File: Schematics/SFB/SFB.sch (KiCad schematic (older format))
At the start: 11 parts, among them J1 JST XH 1x5, SW1 SW_DPST, SW2 SW_DPST, SW3 SW_DPST, U1 Arduino_Nano_v3.x, U2 A1326 LUA-T, U3 A1326 LUA-T, U4 A1326 LUA-T, U5 A1326 LUA-T, U6 A1326 LUA-T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

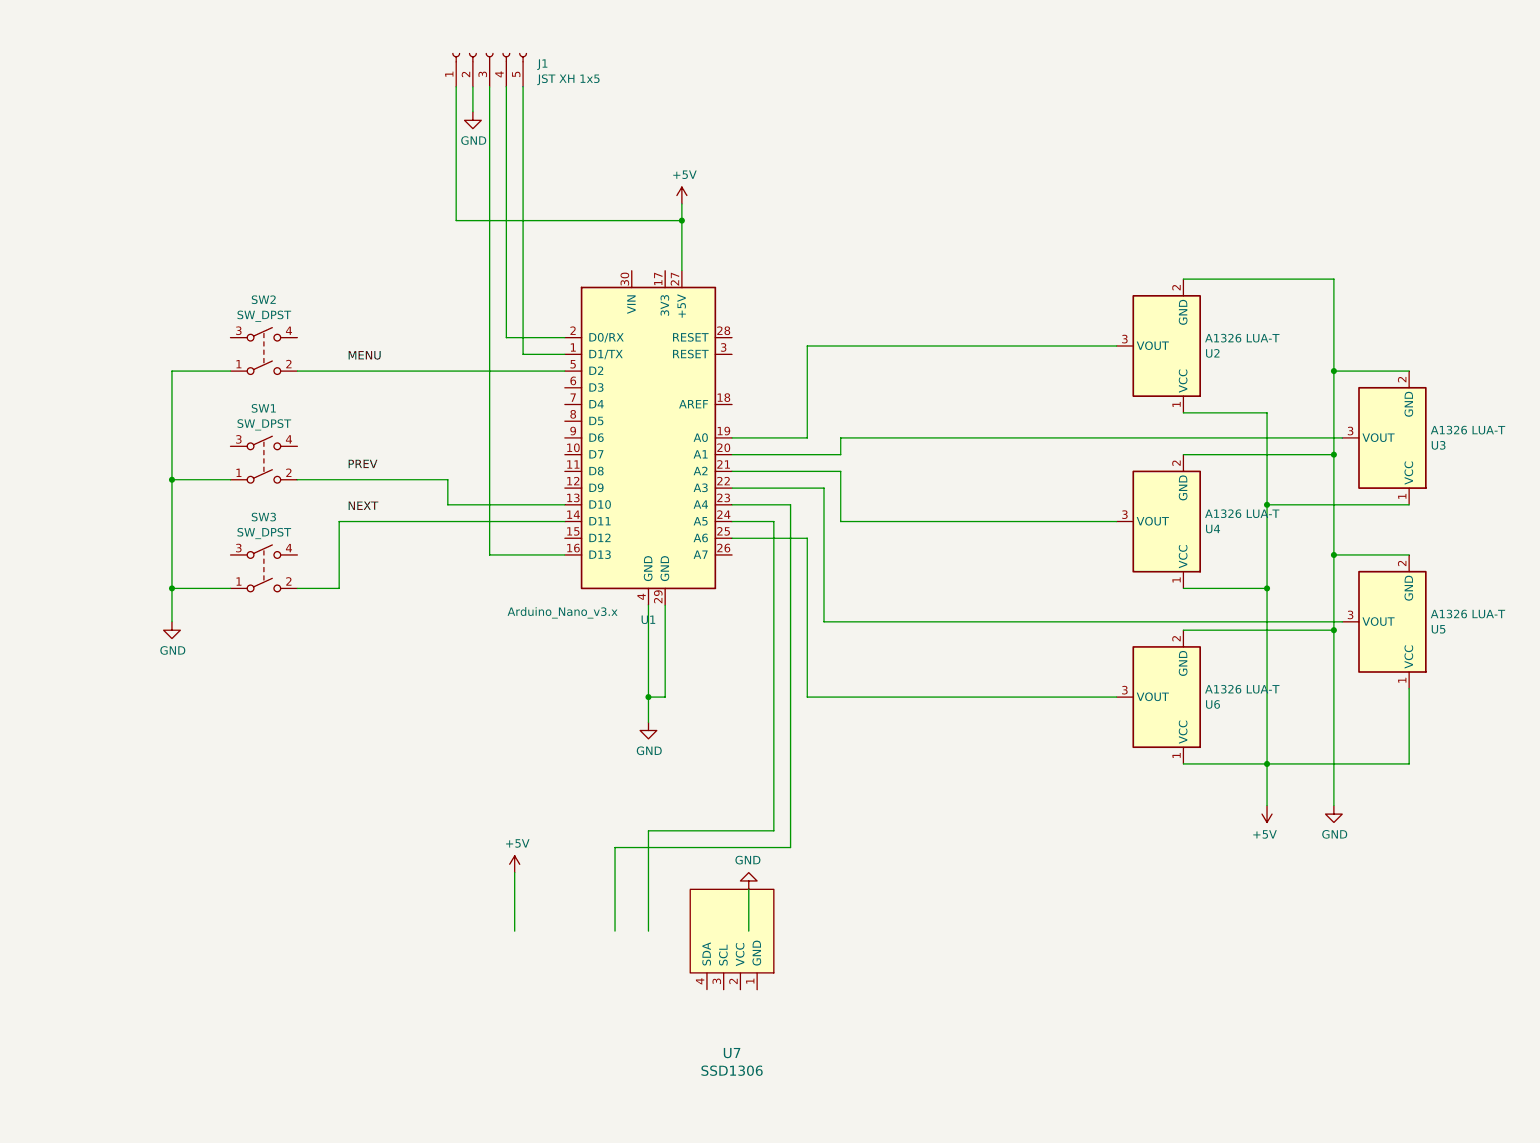
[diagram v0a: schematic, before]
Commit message: Added PCB Rev.2 design
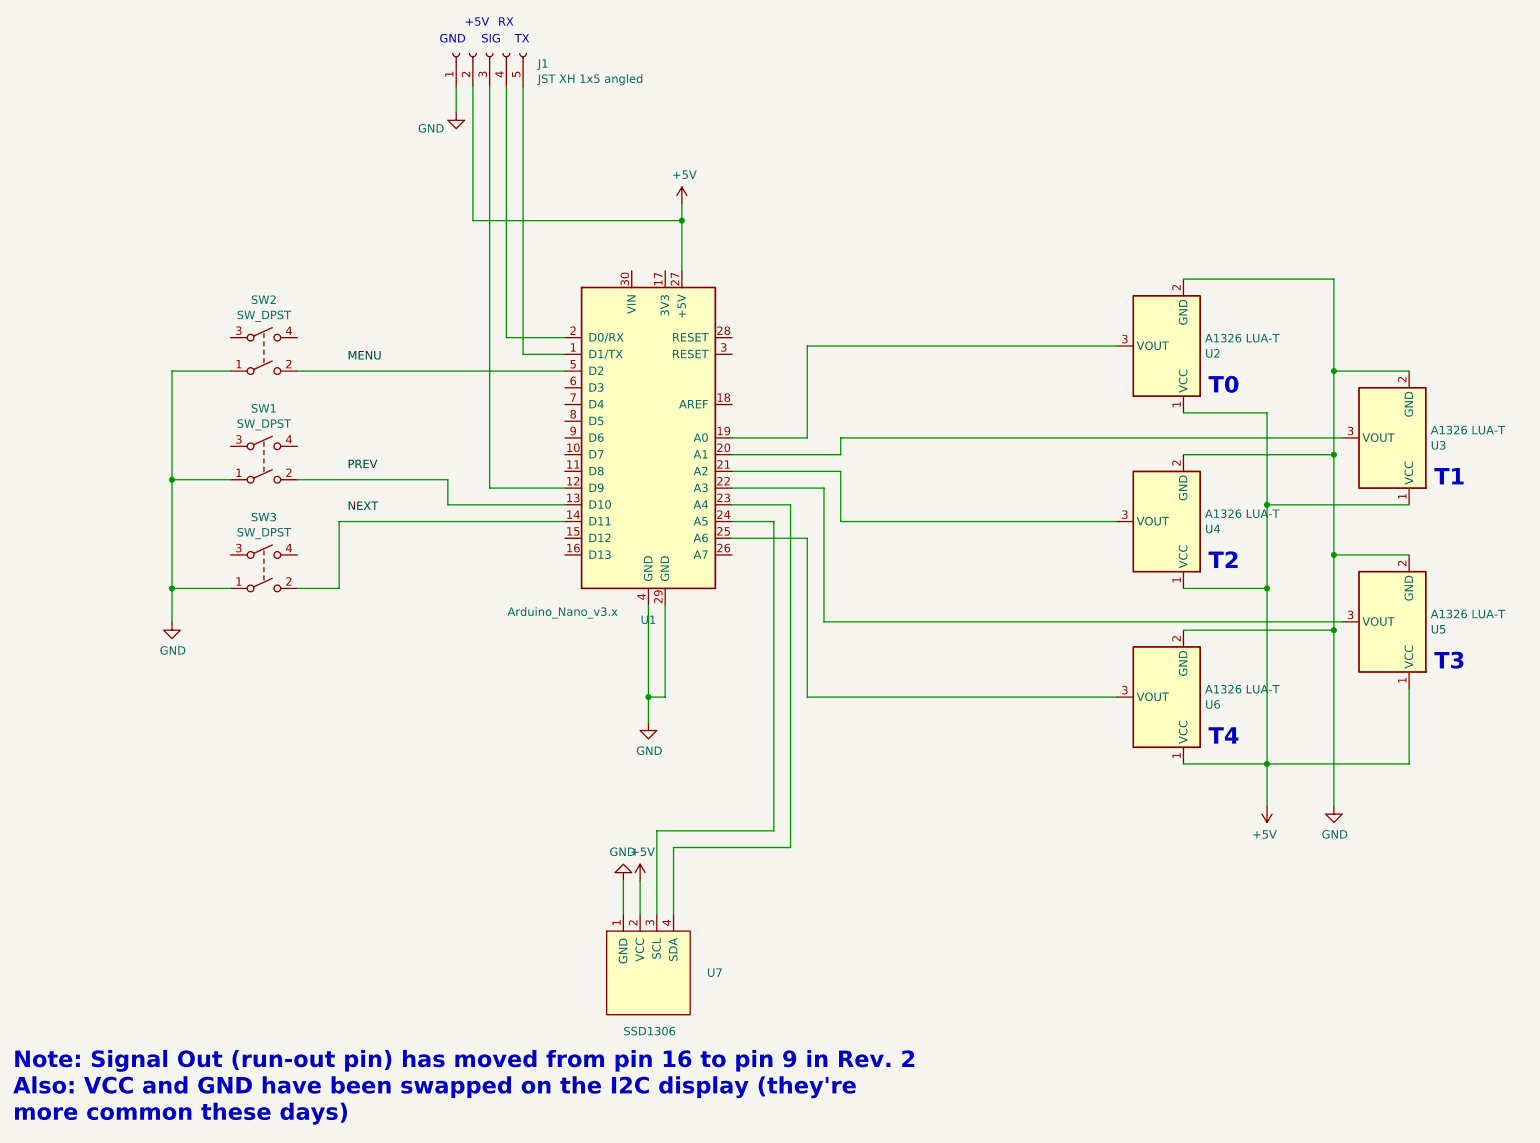
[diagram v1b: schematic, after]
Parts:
- removed U7: SSD1306, symbol SSD1306_OLED-0.91-128x32:SSD1306
- added U7: SSD1306, Connector_PinHeader_2.54mm:PinHeader_1x04_P2.54mm_Vertical, symbol SFB-rescue:SSD1306
- J1: value JST XH 1x5 -> JST XH 1x5 angled; footprint (none) -> Connector_JST:JST_XH_S5B-XH-A_1x05_P2.50mm_Horizontal
- SW1, SW2, SW3: footprint (none) -> SFB:SW_Tactile_Straight_KSA0Axx1LFTR-4Pin
- U2, U3, U4, U5, U6: footprint (none) -> Package_TO_SOT_THT:TO-92Flat
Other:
- note added: "+5V"
- note added: "GND\n"
- note added: "Note: Signal Out (run-out pin) has moved from pin 16 to pin 9 in Rev. 2\nAlso: VCC and GND have been swapped on the I2C display (they're \nmore common these days)"
- note added: "RX"
- note added: "SIG"
- note added: "T0"
- note added: "T1\n"
- note added: "T2"
- note added: "T3"
- note added: "T4"
- note added: "TX"
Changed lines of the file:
@@
 EESchema Schematic File Version 4
+LIBS:SFB-cache
 EELAYER 29 0
 EELAYER END
@@
 Title "Smart Filament Buffer"
 Date "2019-06-24"
-Rev "1"
+Rev "2"
 Comp "Technik Gegg"
 Comment1 ""
@@
 F 0 "U2" H 7321 3096 50  0000 R CNN
 F 1 "A1326 LUA-T" H 7321 3005 50  0000 R CNN
-F 2 "" H 7550 2700 50  0001 L CIN
+F 2 "Package_TO_SOT_THT:TO-92Flat" H 7550 2700 50  0001 L CIN
 F 3 "http://www.allegromicro.com/~/media/Files/Datasheets/A1301-2-Datasheet.ashx" H 7450 3050 50  0001 C CNN
 	1    7550 3050
@@
 F 0 "U4" H 7321 4146 50  0000 R CNN
 F 1 "A1326 LUA-T" H 7321 4055 50  0000 R CNN
-F 2 "" H 7550 3750 50  0001 L CIN
+F 2 "Package_TO_SOT_THT:TO-92Flat" H 7550 3750 50  0001 L CIN
 F 3 "http://www.allegromicro.com/~/media/Files/Datasheets/A1301-2-Datasheet.ashx" H 7450 4100 50  0001 C CNN
 	1    7550 4100
@@
 F 0 "U6" H 7321 5196 50  0000 R CNN
 F 1 "A1326 LUA-T" H 7321 5105 50  0000 R CNN
-F 2 "" H 7550 4800 50  0001 L CIN
+F 2 "Package_TO_SOT_THT:TO-92Flat" H 7550 4800 50  0001 L CIN
 F 3 "http://www.allegromicro.com/~/media/Files/Datasheets/A1301-2-Datasheet.ashx" H 7450 5150 50  0001 C CNN
 	1    7550 5150
@@
 F 0 "U3" H 8671 3646 50  0000 R CNN
 F 1 "A1326 LUA-T" H 8671 3555 50  0000 R CNN
-F 2 "" H 8900 3250 50  0001 L CIN
+F 2 "Package_TO_SOT_THT:TO-92Flat" H 8900 3250 50  0001 L CIN
 F 3 "http://www.allegromicro.com/~/media/Files/Datasheets/A1301-2-Datasheet.ashx" H 8800 3600 50  0001 C CNN
 	1    8900 3600
@@
 F 0 "U5" H 8671 4746 50  0000 R CNN
 F 1 "A1326 LUA-T" H 8671 4655 50  0000 R CNN
-F 2 "" H 8900 4350 50  0001 L CIN
+F 2 "Package_TO_SOT_THT:TO-92Flat" H 8900 4350 50  0001 L CIN
 F 3 "http://www.allegromicro.com/~/media/Files/Datasheets/A1301-2-Datasheet.ashx" H 8800 4700 50  0001 C CNN
 	1    8900 4700
@@
 $EndComp
 $Comp
-L power:GND #PWR?
+L power:GND #PWR0101
 U 1 1 5D10FB78
 P 8550 5800
-F 0 "#PWR?" H 8550 5550 50  0001 C CNN
+F 0 "#PWR0101" H 8550 5550 50  0001 C CNN
 F 1 "GND" H 8555 5627 50  0000 C CNN
 F 2 "" H 8550 5800 50  0001 C CNN
@@
 $EndComp
 $Comp
-L power:GND #PWR?
+L power:GND #PWR0102
 U 1 1 5D11026E
 P 4450 5300
-F 0 "#PWR?" H 4450 5050 50  0001 C CNN
+F 0 "#PWR0102" H 4450 5050 50  0001 C CNN
 F 1 "GND" H 4455 5127 50  0000 C CNN
 F 2 "" H 4450 5300 50  0001 C CNN
@@
 	5400 4200 4950 4200
 $Comp
-L power:+5V #PWR?
+L power:+5V #PWR0103
 U 1 1 5D1137CF
 P 8150 5800
-F 0 "#PWR?" H 8150 5650 50  0001 C CNN
+F 0 "#PWR0103" H 8150 5650 50  0001 C CNN
 F 1 "+5V" H 8165 5973 50  0000 C CNN
 F 2 "" H 8150 5800 50  0001 C CNN
@@
 Connection ~ 4450 5150
 $Comp
-L power:+5V #PWR?
+L power:+5V #PWR0104
 U 1 1 5D119368
 P 4650 2200
-F 0 "#PWR?" H 4650 2050 50  0001 C CNN
+F 0 "#PWR0104" H 4650 2050 50  0001 C CNN
 F 1 "+5V" H 4665 2373 50  0000 C CNN
 F 2 "" H 4650 2200 50  0001 C CNN
@@
 	1    0    0    -1
 $EndComp
-$Comp
-L SSD1306_OLED-0.91-128x32:SSD1306 U7
-U 1 1 5D11F7B3
-P 4950 6550
-F 0 "U7" H 4950 7281 60  0000 C CNN
-F 1 "SSD1306" H 4950 7387 60  0000 C CNN
-F 2 "" H 4950 6550 60  0001 C CNN
-F 3 "" H 4950 6550 60  0001 C CNN
-	1    4950 6550
-	-1   0    0    1
-$EndComp
 Wire Wire Line
 	4950 4000 5300 4000
@@
 	5300 4000 5300 6050
 Wire Wire Line
-	5300 6050 4250 6050
-Wire Wire Line
-	4250 6050 4250 6550
-Wire Wire Line
 	4950 4100 5200 4100
 Wire Wire Line
 	5200 4100 5200 5950
-Wire Wire Line
-	5200 5950 4450 5950
-Wire Wire Line
-	4450 5950 4450 6550
-$Comp
-L power:+5V #PWR?
+$Comp
+L power:+5V #PWR0105
 U 1 1 5D12279F
-P 3650 6200
-F 0 "#PWR?" H 3650 6050 50  0001 C CNN
-F 1 "+5V" H 3665 6373 50  0000 C CNN
-F 2 "" H 3650 6200 50  0001 C CNN
-F 3 "" H 3650 6200 50  0001 C CNN
-	1    3650 6200
-	1    0    0    -1
-$EndComp
-$Comp
-L power:GND #PWR?
-U 1 1 5D123581
-P 5050 6300
-F 0 "#PWR?" H 5050 6050 50  0001 C CNN
-F 1 "GND" H 5055 6127 50  0000 C CNN
-F 2 "" H 5050 6300 50  0001 C CNN
-F 3 "" H 5050 6300 50  0001 C CNN
-	1    5050 6300
-	-1   0    0    1
-$EndComp
-Wire Wire Line
-	5050 6300 5050 6550
-Wire Wire Line
-	3650 6200 3650 6550
+P 4400 6250
+F 0 "#PWR0105" H 4400 6100 50  0001 C CNN
+F 1 "+5V" H 4415 6423 50  0000 C CNN
+F 2 "" H 4400 6250 50  0001 C CNN
+F 3 "" H 4400 6250 50  0001 C CNN
+	1    4400 6250
+	1    0    0    -1
+$EndComp
 $Comp
 L Switch:SW_DPST SW2
@@
 F 0 "SW2" H 2150 3425 50  0000 C CNN
 F 1 "SW_DPST" H 2150 3334 50  0000 C CNN
-F 2 "" H 2150 3100 50  0001 C CNN
+F 2 "SFB:SW_Tactile_Straight_KSA0Axx1LFTR-4Pin" H 2150 3100 50  0001 C CNN
 F 3 "~" H 2150 3100 50  0001 C CNN
 	1    2150 3100
@@
 F 0 "SW1" H 2150 4075 50  0000 C CNN
 F 1 "SW_DPST" H 2150 3984 50  0000 C CNN
-F 2 "" H 2150 3750 50  0001 C CNN
+F 2 "SFB:SW_Tactile_Straight_KSA0Axx1LFTR-4Pin" H 2150 3750 50  0001 C CNN
 F 3 "~" H 2150 3750 50  0001 C CNN
 	1    2150 3750
@@
 F 0 "SW3" H 2150 4725 50  0000 C CNN
 F 1 "SW_DPST" H 2150 4634 50  0000 C CNN
-F 2 "" H 2150 4400 50  0001 C CNN
+F 2 "SFB:SW_Tactile_Straight_KSA0Axx1LFTR-4Pin" H 2150 4400 50  0001 C CNN
 F 3 "~" H 2150 4400 50  0001 C CNN
 	1    2150 4400
@@
 	3950 4100 2600 4100
 $Comp
-L power:GND #PWR?
+L power:GND #PWR0107
 U 1 1 5D12BBE9
 P 1600 4700
-F 0 "#PWR?" H 1600 4450 50  0001 C CNN
+F 0 "#PWR0107" H 1600 4450 50  0001 C CNN
 F 1 "GND" H 1605 4527 50  0000 C CNN
 F 2 "" H 1600 4700 50  0001 C CNN
@@
 P 3500 1300
 F 0 "J1" V 3438 1012 50  0000 R CNN
-F 1 "JST XH 1x5" V 3347 1012 50  0000 R CNN
-F 2 "" H 3500 1300 50  0001 C CNN
+F 1 "JST XH 1x5 angled" V 3347 1012 50  0000 R CNN
+F 2 "Connector_JST:JST_XH_S5B-XH-A_1x05_P2.50mm_Horizontal" H 3500 1300 50  0001 C CNN
 F 3 "~" H 3500 1300 50  0001 C CNN
 	1    3500 1300
 	0    -1   -1   0
 $EndComp
-$Comp
-L power:GND #PWR?
+Wire Wire Line
+	4650 2200 4650 2300
+Connection ~ 4650 2300
+Wire Wire Line
+	4650 2300 4650 2600
+Wire Wire Line
+	3600 1500 3600 3000
+Wire Wire Line
+	3600 3000 3950 3000
+Wire Wire Line
+	3700 1500 3700 3100
+Wire Wire Line
+	3700 3100 3950 3100
+Wire Wire Line
+	3500 1500 3500 3900
+Wire Wire Line
+	4500 5950 4500 6450
+Wire Wire Line
+	4600 6050 4600 6450
+Wire Wire Line
+	4500 5950 5200 5950
+Wire Wire Line
+	4600 6050 5300 6050
+$Comp
+L power:GND #PWR0108
 U 1 1 5D139CC1
-P 3400 1650
-F 0 "#PWR?" H 3400 1400 50  0001 C CNN
-F 1 "GND" H 3405 1477 50  0000 C CNN
-F 2 "" H 3400 1650 50  0001 C CNN
-F 3 "" H 3400 1650 50  0001 C CNN
-	1    3400 1650
-	1    0    0    -1
-$EndComp
-Wire Wire Line
-	4650 2200 4650 2300
-Wire Wire Line
-	3400 1500 3400 1650
-Wire Wire Line
-	3300 1500 3300 2300
-Wire Wire Line
-	3300 2300 4650 2300
-Connection ~ 4650 2300
-Wire Wire Line
-	4650 2300 4650 2600
-Wire Wire Line
-	3600 1500 3600 3000
-Wire Wire Line
-	3600 3000 3950 3000
-Wire Wire Line
-	3700 1500 3700 3100
-Wire Wire Line
-	3700 3100 3950 3100
-Wire Wire Line
-	3500 1500 3500 4300
-Wire Wire Line
-	3500 4300 3950 4300
+P 3300 1650
+F 0 "#PWR0108" H 3300 1400 50  0001 C CNN
+F 1 "GND" H 3150 1550 50  0000 C CNN
+F 2 "" H 3300 1650 50  0001 C CNN
+F 3 "" H 3300 1650 50  0001 C CNN
+	1    3300 1650
+	1    0    0    -1
+$EndComp
+Wire Wire Line
+	3400 1500 3400 2300
+Wire Wire Line
+	3400 2300 4650 2300
+Wire Wire Line
+	3300 1500 3300 1650
+Wire Wire Line
+	3950 3900 3500 3900
+Text Notes 3200 1250 0    50   ~ 0
+GND\n
+Text Notes 3350 1150 0    50   ~ 0
++5V
+Text Notes 3450 1250 0    50   ~ 0
+SIG
+Text Notes 3550 1150 0    50   ~ 0
+RX
+Text Notes 3650 1250 0    50   ~ 0
+TX
+Text Notes 7800 3350 0    98   ~ 20
+T0
+Text Notes 9150 3900 0    98   ~ 20
+T1\n
+Text Notes 7800 4400 0    98   ~ 20
+T2
+Text Notes 9150 5000 0    98   ~ 20
+T3
+Text Notes 7800 5450 0    98   ~ 20
+T4
+$Comp
+L power:GND #PWR0106
+U 1 1 5D123581
+P 4300 6250
+F 0 "#PWR0106" H 4300 6000 50  0001 C CNN
+F 1 "GND" H 4305 6077 50  0000 C CNN
+F 2 "" H 4300 6250 50  0001 C CNN
+F 3 "" H 4300 6250 50  0001 C CNN
+	1    4300 6250
+	-1   0    0    1
+$EndComp
+$Comp
+L SFB-rescue:SSD1306 U7
+U 1 1 5F288751
+P 4450 6800
+F 0 "U7" H 4800 6800 50  0000 L CNN
+F 1 "SSD1306" H 4300 6450 50  0000 L CNN
+F 2 "Connector_PinHeader_2.54mm:PinHeader_1x04_P2.54mm_Vertical" H 4450 7050 50  0001 C CNN
+F 3 "" H 4450 7050 50  0001 C CNN
+	1    4450 6800
+	1    0    0    -1
+$EndComp
+Wire Wire Line
+	4300 6250 4300 6450
+Wire Wire Line
+	4400 6250 4400 6450
+Text Notes 650  7700 0    98   ~ 20
+Note: Signal Out (run-out pin) has moved from pin 16 to pin 9 in Rev. 2\nAlso: VCC and GND have been swapped on the I2C display (they're \nmore common these days)
 $EndSCHEMATC
